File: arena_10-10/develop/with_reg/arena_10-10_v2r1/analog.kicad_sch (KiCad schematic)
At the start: 38 parts, among them J27 Conn_Coaxial, J28 Conn_Coaxial, J29 Conn_Coaxial, U83 OPA2277, U84 REF102AU, U85 MCP4725xxx-xCH, U86 OPA2277, U87 OPA2277

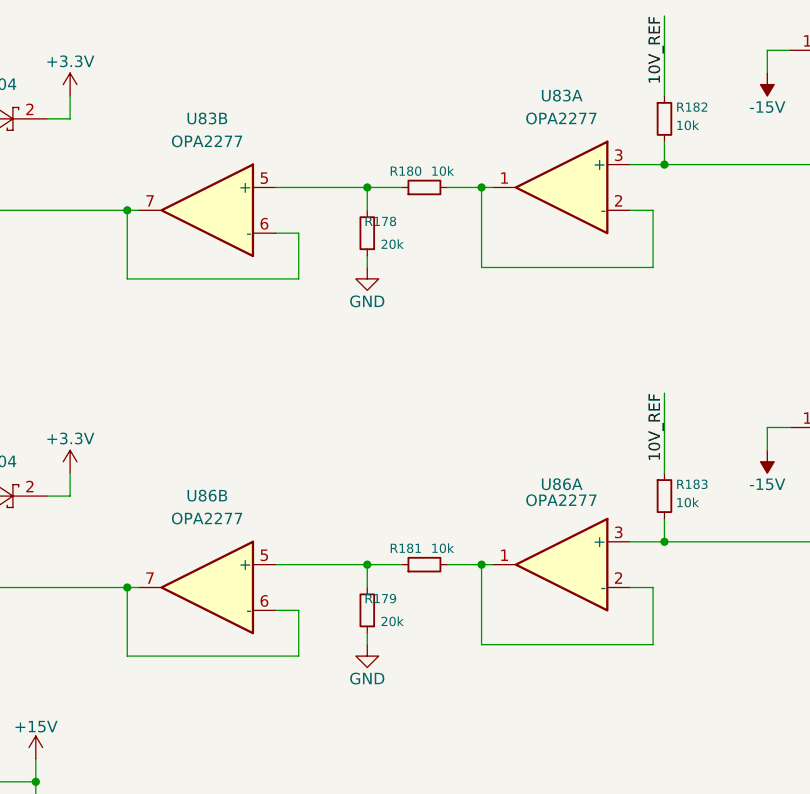
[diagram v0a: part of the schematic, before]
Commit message: Modified notes, moved XT30 connectors.
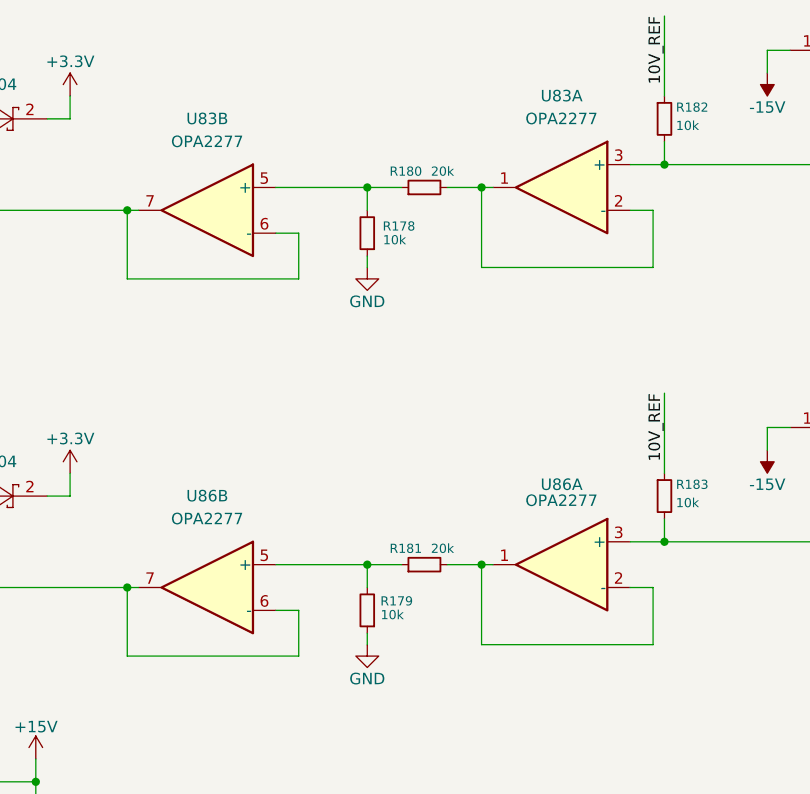
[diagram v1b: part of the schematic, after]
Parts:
- R178, R179: value 20k -> 10k; LCSC Part # C705630 -> C190095
- R180, R181: value 10k -> 20k; LCSC Part # C190095 -> C705630
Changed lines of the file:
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@@
 		(dnp no)
 		(property "Reference" "R179"
-			(at 107.442 125.73 0)
+			(at 109.22 125.984 0)
 			(show_name no)
 			(do_not_autoplace no)
@@
 			)
 		)
-		(property "Value" "20k"
-			(at 108.204 128.27 0)
+		(property "Value" "10k"
+			(at 108.204 127.508 0)
 			(show_name no)
 			(do_not_autoplace no)
@@
 			)
 		)
-		(property "LCSC Part #" "C705630 "
+		(property "LCSC Part #" "C190095 "
 			(at 104.14 127 0)
 			(hide yes)
@@
 		(dnp no)
 		(property "Reference" "R178"
-			(at 107.442 83.82 0)
+			(at 109.474 84.328 0)
 			(show_name no)
 			(do_not_autoplace no)
@@
 			)
 		)
-		(property "Value" "20k"
-			(at 108.204 86.36 0)
+		(property "Value" "10k"
+			(at 108.458 85.852 0)
 			(show_name no)
 			(do_not_autoplace no)
@@
 			)
 		)
-		(property "LCSC Part #" "C705630 "
+		(property "LCSC Part #" "C190095 "
 			(at 104.14 85.09 0)
 			(hide yes)
@@
 			)
 		)
-		(property "Value" "10k"
+		(property "Value" "20k"
 			(at 113.792 120.142 90)
 			(show_name no)
@@
 			)
 		)
-		(property "LCSC Part #" "C190095 "
+		(property "LCSC Part #" "C705630 "
 			(at 110.49 121.92 90)
 			(hide yes)
@@
 			)
 		)
-		(property "Value" "10k"
+		(property "Value" "20k"
 			(at 113.792 78.232 90)
 			(show_name no)
@@
 			)
 		)
-		(property "LCSC Part #" "C190095 "
+		(property "LCSC Part #" "C705630 "
 			(at 110.49 80.01 90)
 			(hide yes)
